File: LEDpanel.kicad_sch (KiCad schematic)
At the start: 107 parts, among them J1 Barrel_Jack_Switch, J2 Barrel_Jack_Switch, J3 Conn_01x02, SW1 SW_SPST, U1 LM317_TO-252, U2 LM317_TO-252, U3 LM317_TO-252, U4 LM317_TO-252, U5 LM317_TO-252, U6 LM317_TO-252

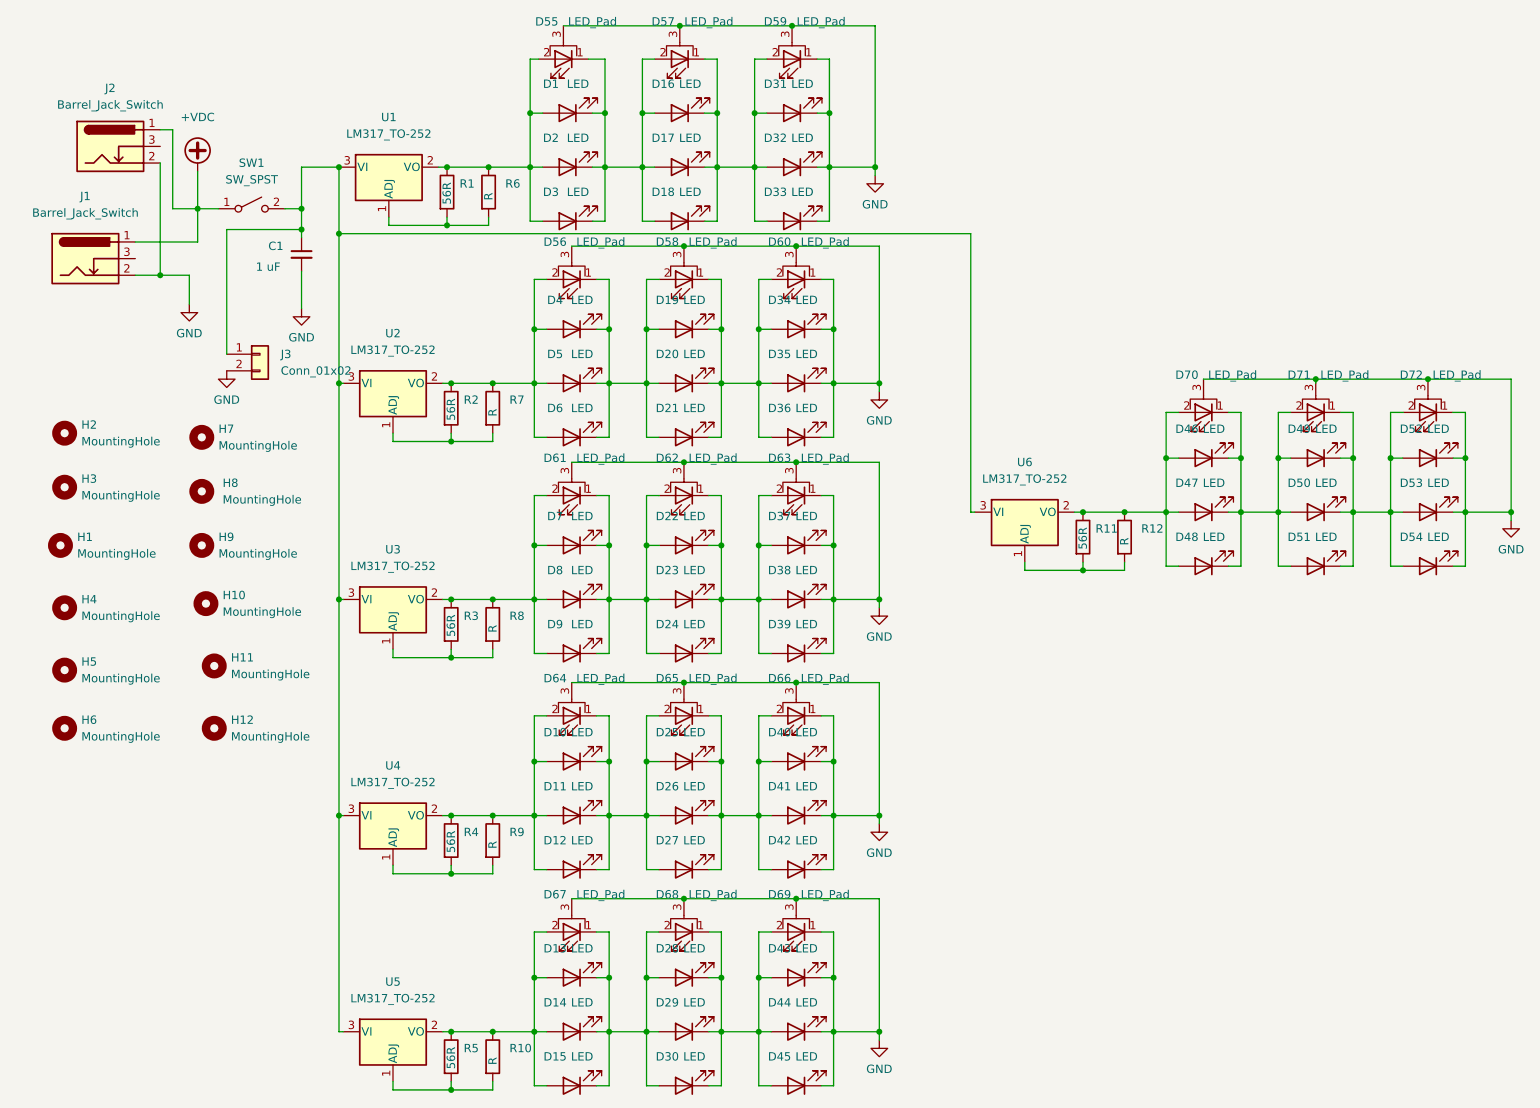
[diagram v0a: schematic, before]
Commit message: Distributed the components somewhat better
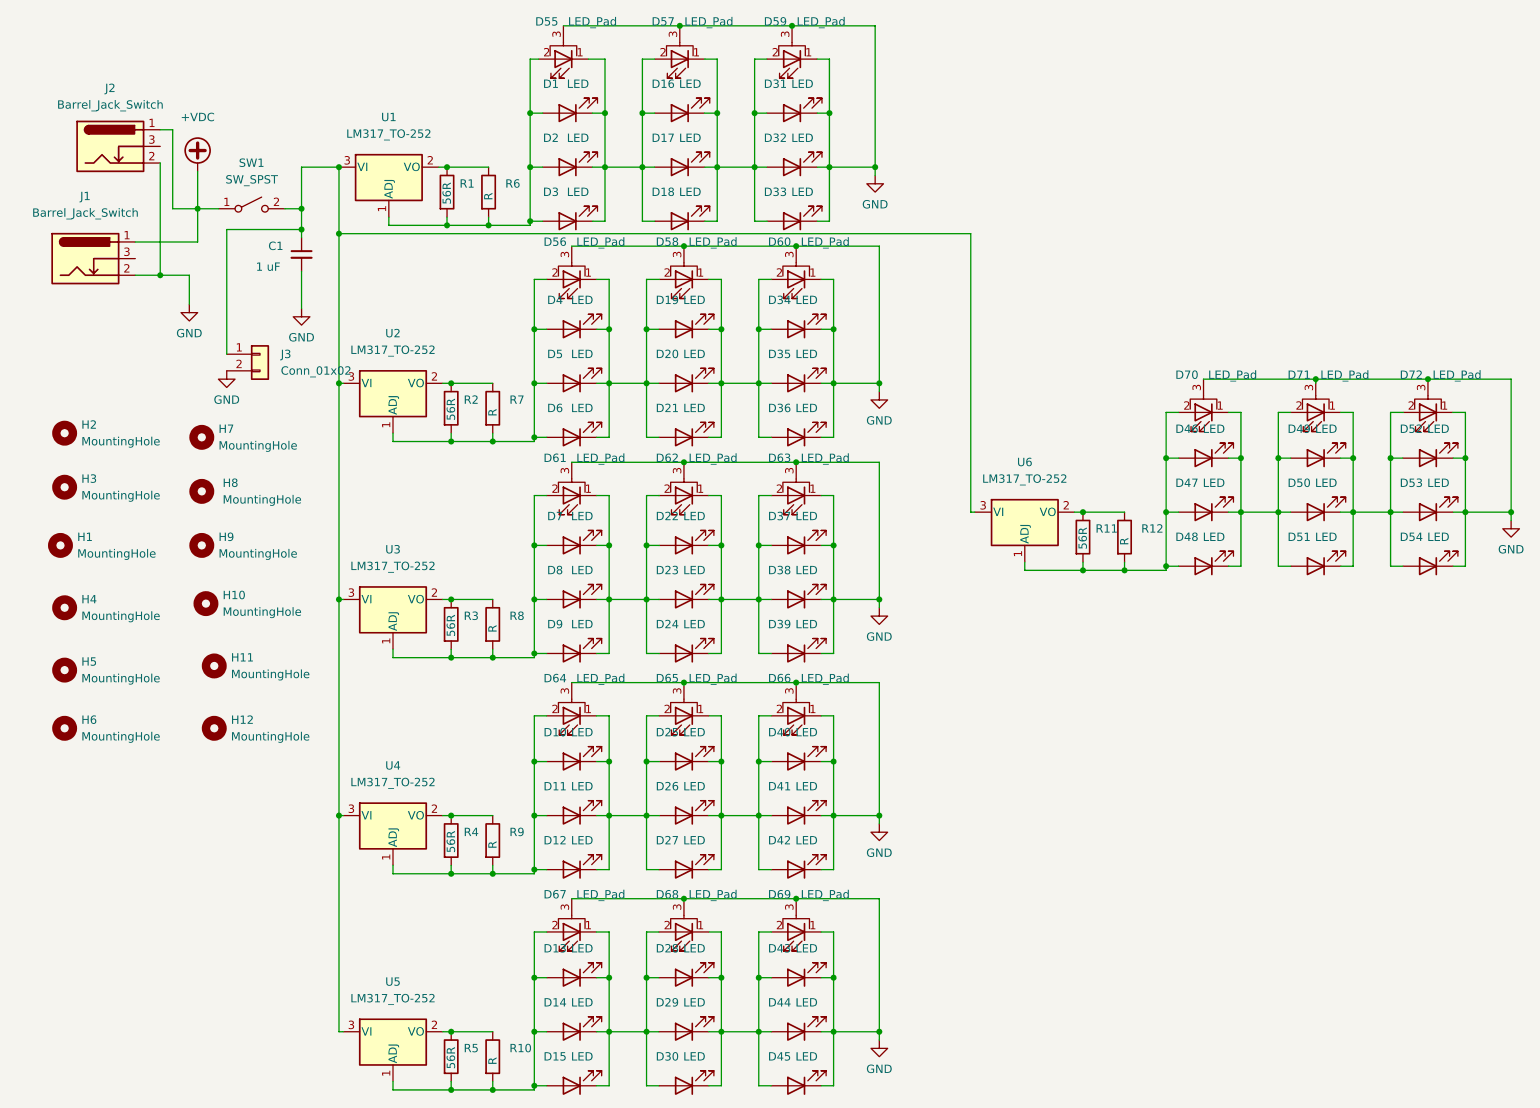
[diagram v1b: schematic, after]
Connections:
- net at D13.2 (A), D14.2 (A), D15.2 (A)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: now also R10.2, R5.2, U5.1 (ADJ); no longer R10.1, R5.1, U5.2 (VO)
- net at D10.2 (A), D11.2 (A), D12.2 (A)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: now also R4.2, R9.2, U4.1 (ADJ); no longer R4.1, R9.1, U4.2 (VO)
- net at D61.2 (A), D7.2 (A), D8.2 (A)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: now also R3.2, R8.2, U3.1 (ADJ); no longer R3.1, R8.1, U3.2 (VO)
- net at D4.2 (A), D5.2 (A), D56.2 (A)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: now also R2.2, R7.2, U2.1 (ADJ); no longer R2.1, R7.1, U2.2 (VO)
- net at D46.2 (A), D47.2 (A), D48.2 (A)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: now also R11.2, R12.2, U6.1 (ADJ); no longer R11.1, R12.1, U6.2 (VO)
- net at D1.2 (A), D2.2 (A), D3.2 (A)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: now also R1.2, R6.2, U1.1 (ADJ); no longer R1.1, R6.1, U1.2 (VO)
- new net: R3.1, R8.1, U3.2 (VO)
- new net: R4.1, R9.1, U4.2 (VO)
- new net: R11.1, R12.1, U6.2 (VO)
- new net: R10.1, R5.1, U5.2 (VO)
- new net: R1.1, R6.1, U1.2 (VO)
- new net: R2.1, R7.1, U2.2 (VO)
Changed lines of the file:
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@@
   (junction (at 145.415 139.065) (diameter 0) (color 0 0 0 0)
   )
+  (junction (at 99.695 89.535) (diameter 0) (color 0 0 0 0)
+  )
   (junction (at 128.27 106.045) (diameter 0) (color 0 0 0 0)
   )
@@
   (junction (at 64.135 57.785) (diameter 0) (color 0 0 0 0)
   )
-  (junction (at 93.345 114.3) (diameter 0) (color 0 0 0 0)
-  )
   (junction (at 116.205 48.26) (diameter 0) (color 0 0 0 0)
   )
+  (junction (at 93.345 123.19) (diameter 0) (color 0 0 0 0)
+  )
   (junction (at 152.4 180.34) (diameter 0) (color 0 0 0 0)
   )
@@
   (junction (at 69.85 147.32) (diameter 0) (color 0 0 0 0)
   )
+  (junction (at 99.695 188.595) (diameter 0) (color 0 0 0 0)
+  )
   (junction (at 145.415 81.28) (diameter 0) (color 0 0 0 0)
   )
   (junction (at 111.125 172.085) (diameter 0) (color 0 0 0 0)
   )
-  (junction (at 93.345 147.32) (diameter 0) (color 0 0 0 0)
-  )
   (junction (at 122.555 127) (diameter 0) (color 0 0 0 0)
   )
@@
   (junction (at 116.205 40.005) (diameter 0) (color 0 0 0 0)
   )
+  (junction (at 99.695 155.575) (diameter 0) (color 0 0 0 0)
+  )
   (junction (at 230.505 92.71) (diameter 0) (color 0 0 0 0)
   )
@@
   (junction (at 121.92 26.67) (diameter 0) (color 0 0 0 0)
   )
+  (junction (at 99.695 122.555) (diameter 0) (color 0 0 0 0)
+  )
   (junction (at 230.505 100.965) (diameter 0) (color 0 0 0 0)
   )
@@
   (junction (at 219.075 80.645) (diameter 0) (color 0 0 0 0)
   )
-  (junction (at 93.345 81.28) (diameter 0) (color 0 0 0 0)
-  )
   (junction (at 139.065 26.67) (diameter 0) (color 0 0 0 0)
   )
@@
   (junction (at 133.35 40.005) (diameter 0) (color 0 0 0 0)
   )
-  (junction (at 92.71 48.26) (diameter 0) (color 0 0 0 0)
+  (junction (at 196.215 109.22) (diameter 0) (color 0 0 0 0)
+  )
+  (junction (at 93.345 189.23) (diameter 0) (color 0 0 0 0)
   )
   (junction (at 86.995 189.23) (diameter 0) (color 0 0 0 0)
   )
+  (junction (at 93.345 90.17) (diameter 0) (color 0 0 0 0)
+  )
   (junction (at 116.84 147.32) (diameter 0) (color 0 0 0 0)
   )
@@
   (junction (at 111.125 139.065) (diameter 0) (color 0 0 0 0)
   )
+  (junction (at 99.06 56.515) (diameter 0) (color 0 0 0 0)
+  )
   (junction (at 133.985 147.32) (diameter 0) (color 0 0 0 0)
   )
@@
   (junction (at 128.27 147.32) (diameter 0) (color 0 0 0 0)
   )
-  (junction (at 93.345 180.34) (diameter 0) (color 0 0 0 0)
-  )
   (junction (at 86.995 123.19) (diameter 0) (color 0 0 0 0)
   )
@@
   (junction (at 69.85 81.28) (diameter 0) (color 0 0 0 0)
   )
+  (junction (at 189.865 109.855) (diameter 0) (color 0 0 0 0)
+  )
   (junction (at 128.27 180.34) (diameter 0) (color 0 0 0 0)
   )
@@
   (junction (at 248.92 100.965) (diameter 0) (color 0 0 0 0)
   )
+  (junction (at 93.345 156.21) (diameter 0) (color 0 0 0 0)
+  )
   (junction (at 116.84 81.28) (diameter 0) (color 0 0 0 0)
   )
@@
   (junction (at 86.995 147.32) (diameter 0) (color 0 0 0 0)
   )
+  (junction (at 92.71 57.15) (diameter 0) (color 0 0 0 0)
+  )
   (junction (at 133.985 106.045) (diameter 0) (color 0 0 0 0)
   )
@@
   (junction (at 99.06 48.26) (diameter 0) (color 0 0 0 0)
   )
-  (junction (at 189.865 100.965) (diameter 0) (color 0 0 0 0)
-  )
   (junction (at 86.36 48.26) (diameter 0) (color 0 0 0 0)
   )
@@
     (stroke (width 0) (type default) (color 0 0 0 0))
   )
-  (wire (pts (xy 93.345 114.3) (xy 99.695 114.3))
-    (stroke (width 0) (type default) (color 0 0 0 0))
-  )
   (wire (pts (xy 86.995 189.23) (xy 86.995 187.96))
     (stroke (width 0) (type default) (color 0 0 0 0))
@@
     (stroke (width 0) (type default) (color 0 0 0 0))
   )
+  (wire (pts (xy 99.695 123.19) (xy 99.695 122.555))
+    (stroke (width 0) (type default) (color 0 0 0 0))
+  )
   (wire (pts (xy 183.515 100.965) (xy 182.245 100.965))
     (stroke (width 0) (type default) (color 0 0 0 0))
@@
     (stroke (width 0) (type default) (color 0 0 0 0))
   )
+  (wire (pts (xy 189.865 109.855) (xy 196.215 109.855))
+    (stroke (width 0) (type default) (color 0 0 0 0))
+  )
   (wire (pts (xy 109.22 147.32) (xy 111.125 147.32))
     (stroke (width 0) (type default) (color 0 0 0 0))
@@
     (stroke (width 0) (type default) (color 0 0 0 0))
   )
+  (wire (pts (xy 99.695 156.21) (xy 99.695 155.575))
+    (stroke (width 0) (type default) (color 0 0 0 0))
+  )
   (wire (pts (xy 144.78 40.005) (xy 144.78 48.26))
     (stroke (width 0) (type default) (color 0 0 0 0))
@@
     (stroke (width 0) (type default) (color 0 0 0 0))
   )
+  (wire (pts (xy 99.695 90.17) (xy 99.695 89.535))
+    (stroke (width 0) (type default) (color 0 0 0 0))
+  )
   (wire (pts (xy 116.84 132.08) (xy 118.745 132.08))
     (stroke (width 0) (type default) (color 0 0 0 0))
@@
     (stroke (width 0) (type default) (color 0 0 0 0))
   )
-  (wire (pts (xy 189.865 100.965) (xy 196.215 100.965))
-    (stroke (width 0) (type default) (color 0 0 0 0))
-  )
   (wire (pts (xy 116.205 56.515) (xy 118.11 56.515))
     (stroke (width 0) (type default) (color 0 0 0 0))
@@
     (stroke (width 0) (type default) (color 0 0 0 0))
   )
+  (wire (pts (xy 93.345 123.19) (xy 99.695 123.19))
+    (stroke (width 0) (type default) (color 0 0 0 0))
+  )
   (wire (pts (xy 86.995 81.28) (xy 93.345 81.28))
     (stroke (width 0) (type default) (color 0 0 0 0))
@@
     (stroke (width 0) (type default) (color 0 0 0 0))
   )
+  (wire (pts (xy 93.345 156.21) (xy 99.695 156.21))
+    (stroke (width 0) (type default) (color 0 0 0 0))
+  )
   (wire (pts (xy 111.125 122.555) (xy 109.22 122.555))
     (stroke (width 0) (type default) (color 0 0 0 0))
@@
     (stroke (width 0) (type default) (color 0 0 0 0))
   )
+  (wire (pts (xy 99.695 189.23) (xy 99.695 188.595))
+    (stroke (width 0) (type default) (color 0 0 0 0))
+  )
   (wire (pts (xy 236.22 80.645) (xy 248.92 80.645))
     (stroke (width 0) (type default) (color 0 0 0 0))
@@
     (stroke (width 0) (type default) (color 0 0 0 0))
   )
-  (wire (pts (xy 93.345 81.28) (xy 99.695 81.28))
-    (stroke (width 0) (type default) (color 0 0 0 0))
-  )
   (wire (pts (xy 128.27 98.425) (xy 126.365 98.425))
     (stroke (width 0) (type default) (color 0 0 0 0))
@@
     (stroke (width 0) (type default) (color 0 0 0 0))
   )
+  (wire (pts (xy 99.06 57.15) (xy 99.06 56.515))
+    (stroke (width 0) (type default) (color 0 0 0 0))
+  )
   (wire (pts (xy 133.985 180.34) (xy 133.985 188.595))
     (stroke (width 0) (type default) (color 0 0 0 0))
   )
+  (wire (pts (xy 93.345 90.17) (xy 99.695 90.17))
+    (stroke (width 0) (type default) (color 0 0 0 0))
+  )
   (wire (pts (xy 110.49 48.26) (xy 110.49 56.515))
     (stroke (width 0) (type default) (color 0 0 0 0))
@@
     (stroke (width 0) (type default) (color 0 0 0 0))
   )
-  (wire (pts (xy 93.345 147.32) (xy 99.695 147.32))
-    (stroke (width 0) (type default) (color 0 0 0 0))
-  )
   (wire (pts (xy 116.84 98.425) (xy 118.745 98.425))
     (stroke (width 0) (type default) (color 0 0 0 0))
@@
     (stroke (width 0) (type default) (color 0 0 0 0))
   )
-  (wire (pts (xy 92.71 48.26) (xy 99.06 48.26))
-    (stroke (width 0) (type default) (color 0 0 0 0))
-  )
   (wire (pts (xy 196.215 100.965) (xy 196.215 109.22))
     (stroke (width 0) (type default) (color 0 0 0 0))
@@
     (stroke (width 0) (type default) (color 0 0 0 0))
   )
+  (wire (pts (xy 93.345 189.23) (xy 99.695 189.23))
+    (stroke (width 0) (type default) (color 0 0 0 0))
+  )
   (wire (pts (xy 144.78 40.005) (xy 144.78 31.75))
     (stroke (width 0) (type default) (color 0 0 0 0))
@@
     (stroke (width 0) (type default) (color 0 0 0 0))
   )
+  (wire (pts (xy 92.71 57.15) (xy 99.06 57.15))
+    (stroke (width 0) (type default) (color 0 0 0 0))
+  )
   (wire (pts (xy 99.695 180.34) (xy 101.6 180.34))
     (stroke (width 0) (type default) (color 0 0 0 0))
@@
     (stroke (width 0) (type default) (color 0 0 0 0))
   )
+  (wire (pts (xy 196.215 109.855) (xy 196.215 109.22))
+    (stroke (width 0) (type default) (color 0 0 0 0))
+  )
   (wire (pts (xy 143.51 81.28) (xy 145.415 81.28))
     (stroke (width 0) (type default) (color 0 0 0 0))
@@
     (stroke (width 0) (type default) (color 0 0 0 0))
   )
-  (wire (pts (xy 93.345 180.34) (xy 99.695 180.34))
-    (stroke (width 0) (type default) (color 0 0 0 0))
-  )
